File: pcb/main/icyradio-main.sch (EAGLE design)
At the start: 702 parts, among them CON101 FPC-22P, CON102 FPC-22P, CON1101 2EDG-2P-5MM-H, CON701 4P-SH-TOP, CON801 PCIE-X4-EDGE, J101 RJ45_MAG_LED_1G-TE-1-2301994-0, J701 TRSJACK, J702 TRSJACK, J703 TRSJACK, M701 SPH0641LM4H-1, M702 SPH0641LM4H-1, Q101 AO3400, Q102 AO3400, Q1101 AO3400, Q1102 AO4805, Q1103 AO3400, Q1104 AO4805, Q1105 AO4805, Q1106 AO3400, T501 UWB1-85E, T502 UWB1-85E, T503 UWB1-85E, T504 UWB1-85E, T505 UWB1-85E, T506 UWB1-85E, T507 UWB1-85E, T508 UWB1-85E, U1001 LTC4313-3, U1002 UPD301C, U1003 MIC2019, U101 MIC2019, U102 RPI-CM4, U1101 MCP1804-3302, U1102 LT7182S, U1201 ADM7172ACPZ-5.0, U1202 ADM7171ACPZ-1.3, U1203 ADM7171ACPZ-3.3, U1204 MIC23159, U1205 MIC5166, U1206 ADM7171ACPZ-1.3, U1207 ADM7171ACPZ-3.3, U1208 MIC23159, U1209 MIC23155, U1210 ADP7142AUJZ-3.3, U201 XC7A100TFGG484, U202 SST26VF064B, U301 MT41K256M16TW-125, U401 AD9361, U501 MIC2019, U502 MIC2019, U503 MIC2019, U504 MIC2019, U505 ADL5601, U506 ADL5601, U601 8V97003, U701 ADAU1372, U901 DSB321SDA, U902 SI5351C-B-GM

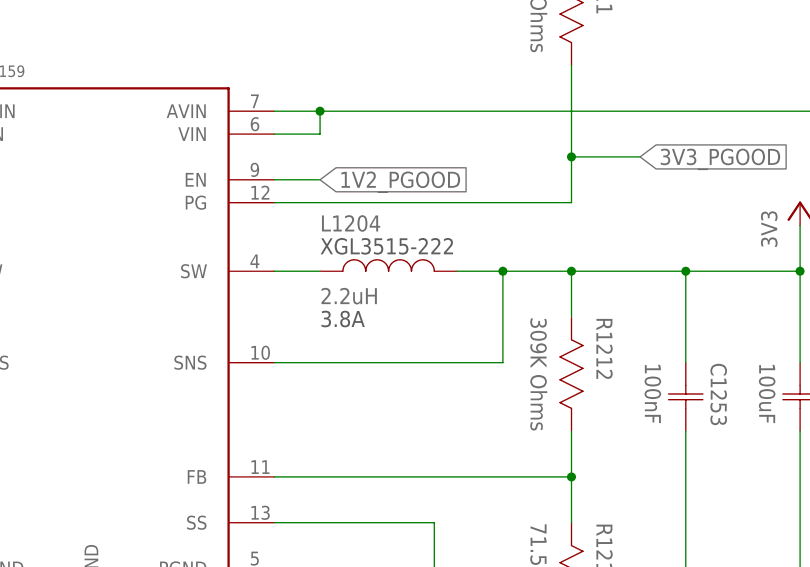
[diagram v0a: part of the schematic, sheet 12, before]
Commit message: pcb: Update 3V3 switching regulator inductor to 4.7 uH so it exits DCM pcb: Update transceiver clock DC-block capacitor to 100nF
Signed-off-by: João Silva <jgc3silva@gmail.com>
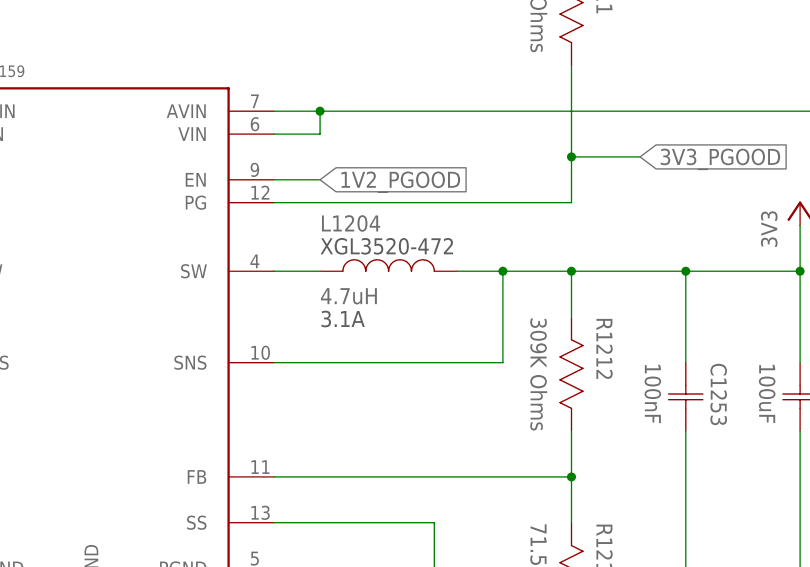
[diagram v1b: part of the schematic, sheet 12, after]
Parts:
- C403: value 10pF -> 100nF
- L1204: value 2.2uH -> 4.7uH; device Coilcraft:XGL3515-222 -> Coilcraft:XGL3520-472; CURRENT 3.8A -> (none)
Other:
- note added: "Flash SCK is connected to CCLK for initial configuration, and also to a dedicated IO, to be used in the design at full speed."
- note removed: "Flash SCK is connecterd to CCLK for initial configuration, and also to a dedicated IO, to be used in the design at full speed."
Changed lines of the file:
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@@
 <part name="GND71" library="Supply Symbol" deviceset="GND" device=""/>
 <part name="GND68" library="Supply Symbol" deviceset="GND" device=""/>
-<part name="C403" library="Capacitor" deviceset="CAPACITOR" device="-0402" value="10pF"/>
+<part name="C403" library="Capacitor" deviceset="CAPACITOR" device="-0402" value="100nF"/>
 <part name="C402" library="Capacitor" deviceset="CAPACITOR" device="-0402" value="DNP"/>
 <part name="GND72" library="Supply Symbol" deviceset="GND" device=""/>
@@
 <part name="M702" library="Knowles" deviceset="SPH0641LM4H-1" device=""/>
 <part name="GND79" library="Supply Symbol" deviceset="GND" device=""/>
-<part name="L1204" library="Coilcraft" deviceset="XGL3515-" device="" technology="222" value="2.2uH">
-<attribute name="CURRENT" value="3.8A"/>
-</part>
+<part name="L1204" library="Coilcraft" deviceset="XGL3520-" device="" technology="472" value="4.7uH"/>
 <part name="L1203" library="Coilcraft" deviceset="XGL3515-" device="" technology="222" value="2.2uH">
 <attribute name="CURRENT" value="3.8A"/>
@@
 <text x="453.644" y="355.6" size="1.27" layer="98" align="center">Pullups as per Xillinx recommendation</text>
 <text x="502.92" y="120.904" size="1.27" layer="98" rot="R90" align="center">Pullups as per Xillinx recommendation</text>
-<text x="390.144" y="325.12" size="1.27" layer="98" align="center">Flash SCK is connecterd to CCLK for initial
+<text x="390.144" y="325.12" size="1.27" layer="98" align="center">Flash SCK is connected to CCLK for initial
 configuration, and also to a dedicated IO,
 to be used in the design at full speed.</text>

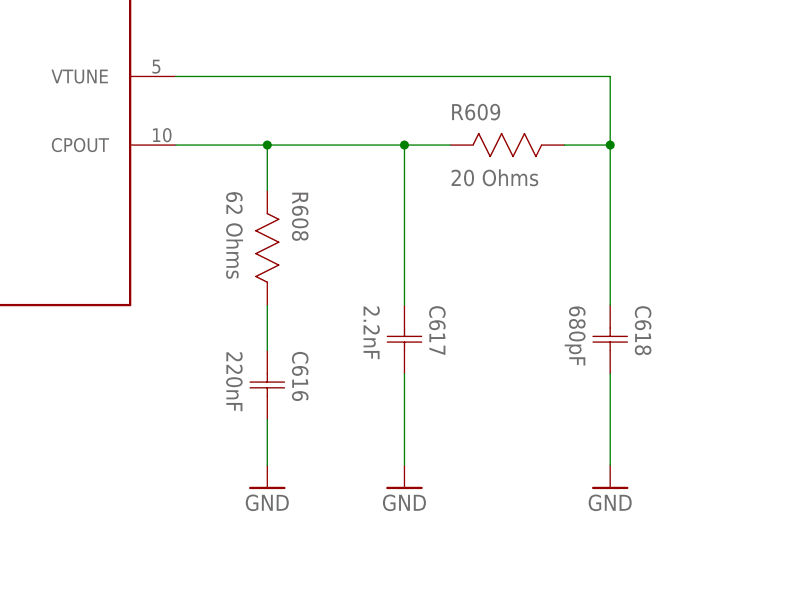
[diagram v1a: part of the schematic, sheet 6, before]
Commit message: pcb: Change mmWave Synth loop filter component values
Signed-off-by: João Silva <jgc3silva@gmail.com>
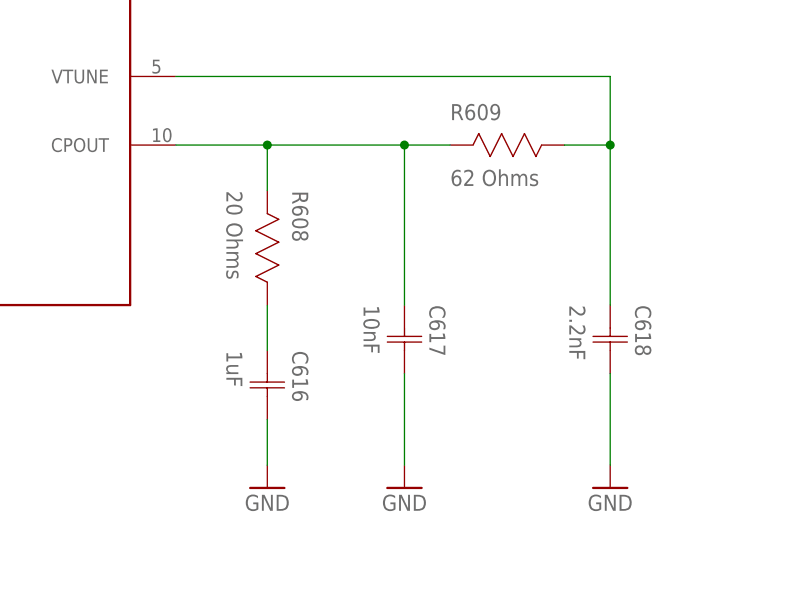
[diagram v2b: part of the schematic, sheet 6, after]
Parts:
- C616: value 220nF -> 1uF
- C617: value 2.2nF -> 10nF
- C618: value 680pF -> 2.2nF
- R608: value 62 Ohms -> 20 Ohms
- R609: value 20 Ohms -> 62 Ohms
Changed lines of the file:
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@@
 <part name="C620" library="Capacitor" deviceset="CAPACITOR" device="-0402" value="10nF"/>
 <part name="GND431" library="Supply Symbol" deviceset="GND" device=""/>
-<part name="R608" library="Resistor" deviceset="RESISTOR" device="-0402" value="62 Ohms"/>
-<part name="C616" library="Capacitor" deviceset="CAPACITOR" device="-0402" value="220nF"/>
-<part name="R609" library="Resistor" deviceset="RESISTOR" device="-0402" value="20 Ohms"/>
-<part name="C617" library="Capacitor" deviceset="CAPACITOR" device="-0402" value="2.2nF"/>
-<part name="C618" library="Capacitor" deviceset="CAPACITOR" device="-0402" value="680pF"/>
+<part name="R608" library="Resistor" deviceset="RESISTOR" device="-0402" value="20 Ohms"/>
+<part name="C616" library="Capacitor" deviceset="CAPACITOR" device="-0402" value="1uF"/>
+<part name="R609" library="Resistor" deviceset="RESISTOR" device="-0402" value="62 Ohms"/>
+<part name="C617" library="Capacitor" deviceset="CAPACITOR" device="-0402" value="10nF"/>
+<part name="C618" library="Capacitor" deviceset="CAPACITOR" device="-0402" value="2.2nF"/>
 <part name="GND432" library="Supply Symbol" deviceset="GND" device=""/>
 <part name="GND433" library="Supply Symbol" deviceset="GND" device=""/>

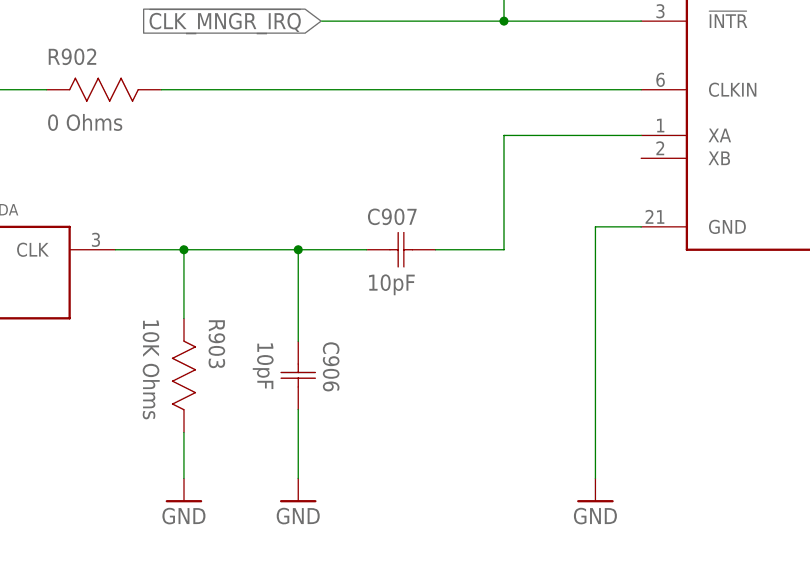
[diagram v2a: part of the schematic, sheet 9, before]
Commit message: pcb: Update TCXO AC couple capacitor to 100nF
Signed-off-by: João Silva <jgc3silva@gmail.com>
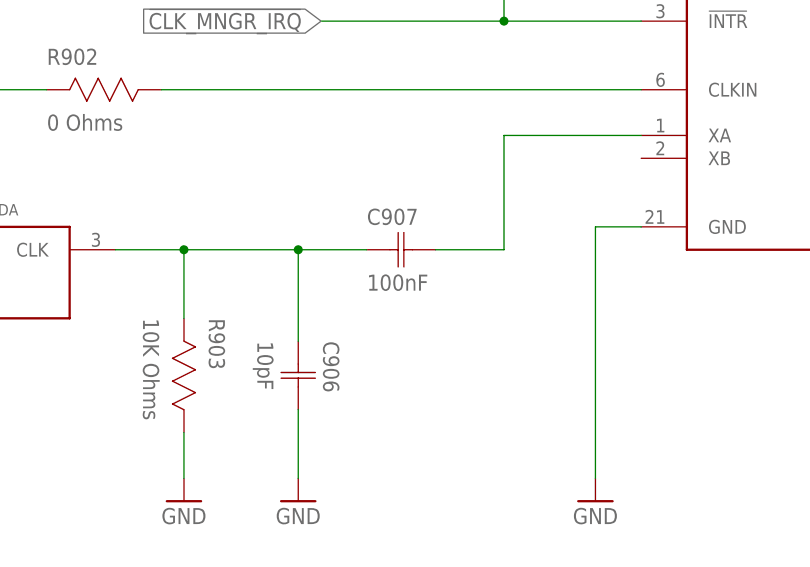
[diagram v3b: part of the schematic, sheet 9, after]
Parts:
- C907: value 10pF -> 100nF
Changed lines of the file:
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@@
 <part name="R903" library="Resistor" deviceset="RESISTOR" device="-0402" value="10K Ohms"/>
 <part name="GND90" library="Supply Symbol" deviceset="GND" device=""/>
-<part name="C907" library="Capacitor" deviceset="CAPACITOR" device="-0402" value="10pF"/>
+<part name="C907" library="Capacitor" deviceset="CAPACITOR" device="-0402" value="100nF"/>
 <part name="RFCON901" library="RF Connector" deviceset="RFCON" device="-U.FL"/>
 <part name="GND91" library="Supply Symbol" deviceset="GND" device=""/>
